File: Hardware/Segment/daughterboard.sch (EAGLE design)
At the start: 162 parts, among them IC1 PBQ79656PAPTQ1, IC2 PBQ79656PAPTQ1, T1 PBHV8115X, 115, T2 PBHV8115X, 115

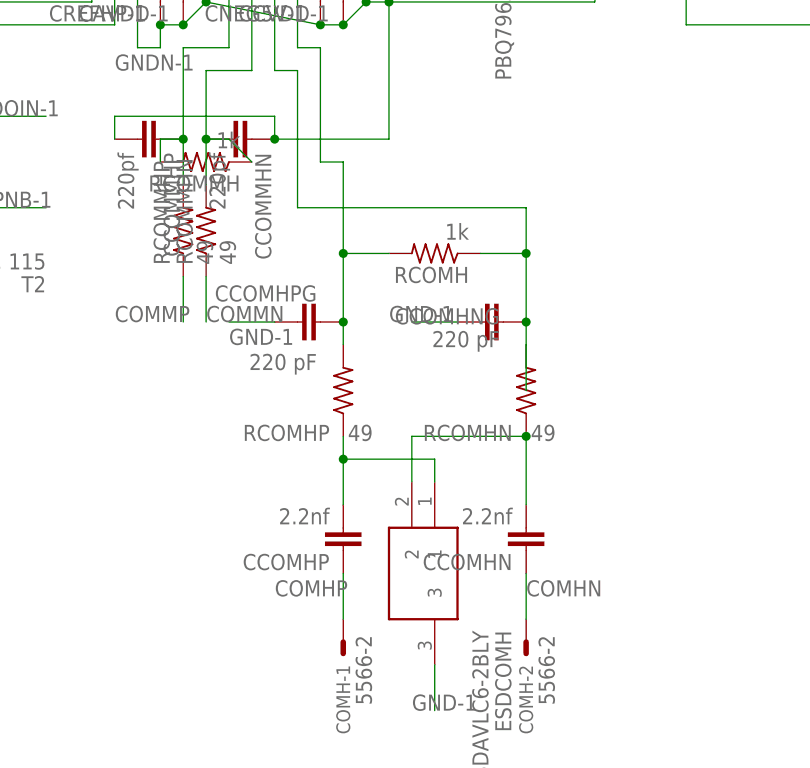
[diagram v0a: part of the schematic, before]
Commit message: Worked on routing daughterboard, mostly finished COM
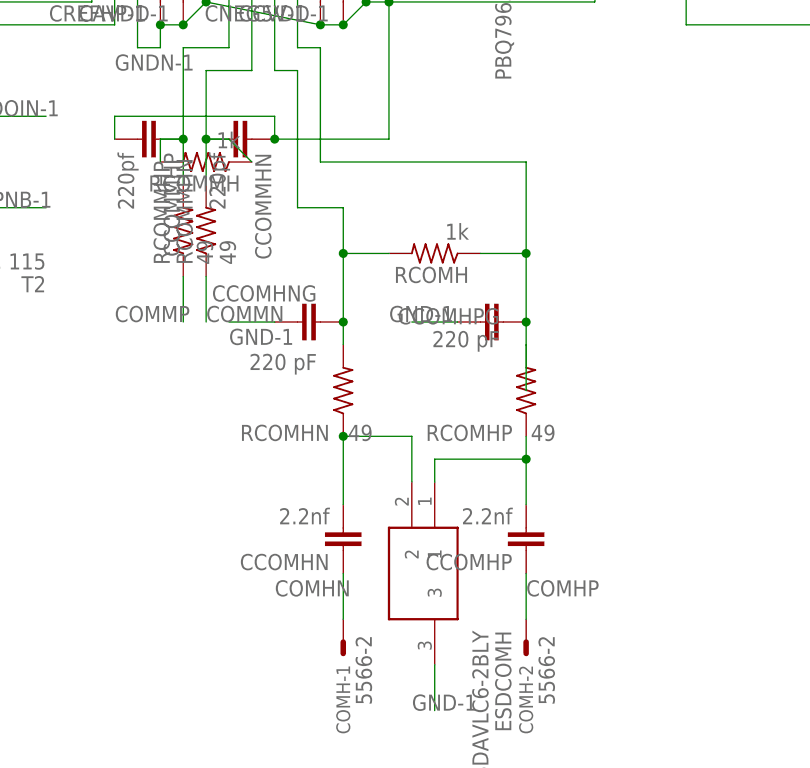
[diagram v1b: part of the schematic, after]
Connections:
- net COMHN: now also COMH-1.S; no longer COMH-2.S
- net COMHP: now also COMH-2.S; no longer COMH-1.S
- net N$131: now also RCOMH.1; no longer RCOMH.2
- net N$132: now also RCOMH.2; no longer RCOMH.1
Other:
- moved on the sheet: CCOMHN, CCOMHNG, CCOMHP, CCOMHPG, RCOMHN, RCOMHP

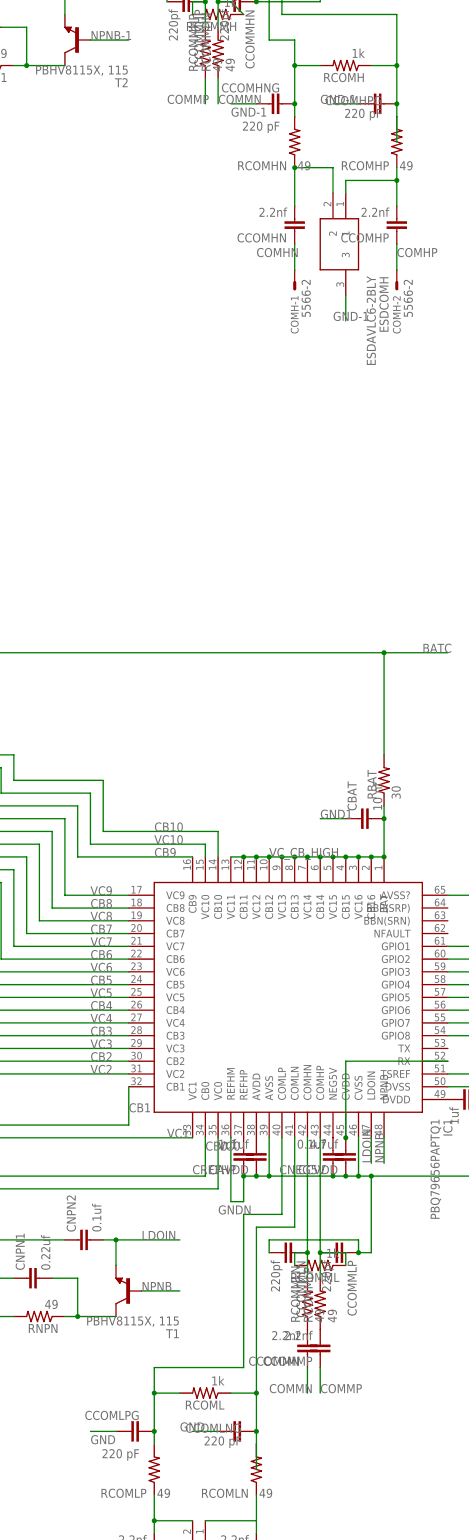
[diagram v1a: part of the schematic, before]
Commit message: Added com isolation to main board
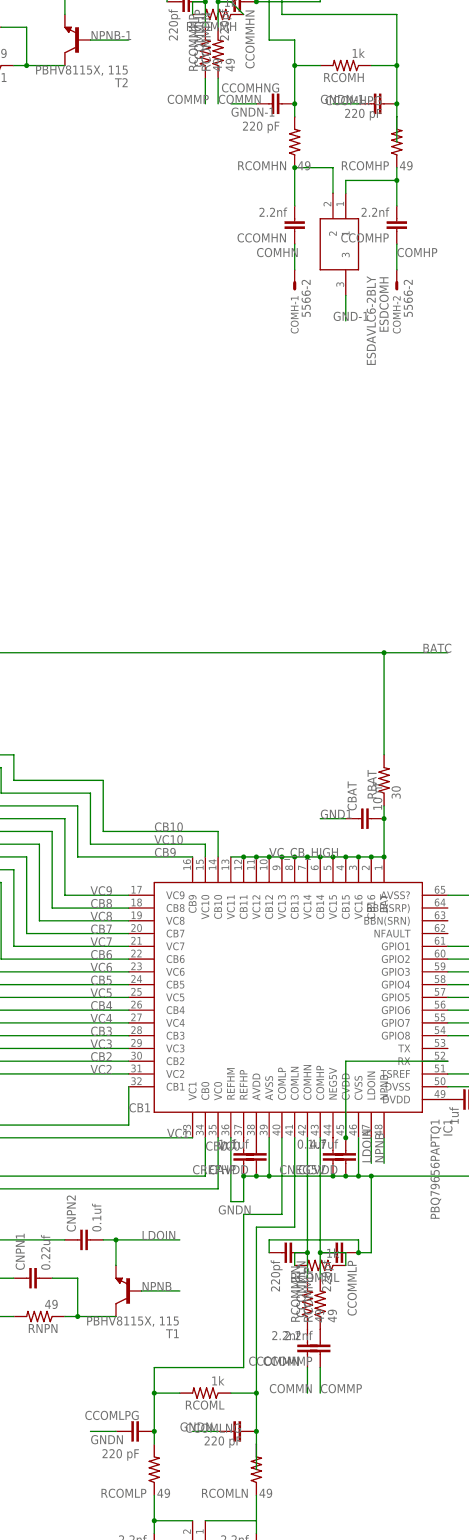
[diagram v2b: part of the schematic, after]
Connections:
- net GND: no longer CCOMLNG.1, CCOMLPG.1
- net GND-1: no longer CCOMHNG.1, CCOMHPG.1
- net GNDN: now also CCOMLNG.1, CCOMLPG.1
- net GNDN-1: now also CCOMHNG.1, CCOMHPG.1
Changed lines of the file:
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@@
 <junction x="175.26" y="20.32"/>
+</segment>
+<segment>
+<wire x1="124.46" y1="-30.48" x2="119.38" y2="-30.48" width="0.1524" layer="91"/>
+<label x="119.38" y="-33.02" size="1.778" layer="95"/>
+<pinref part="CCOMLPG" gate="G$1" pin="1"/>
+</segment>
+<segment>
+<pinref part="CCOMLNG" gate="G$1" pin="1"/>
+<wire x1="144.78" y1="-30.48" x2="139.7" y2="-30.48" width="0.1524" layer="91"/>
+<label x="137.16" y="-30.48" size="1.778" layer="95"/>
 </segment>
 </net>
@@
 <wire x1="104.14" y1="0" x2="93.98" y2="0" width="0.1524" layer="91"/>
 <label x="93.98" y="0" size="1.778" layer="95"/>
-</segment>
-<segment>
-<pinref part="CCOMLNG" gate="G$1" pin="1"/>
-<wire x1="144.78" y1="-30.48" x2="139.7" y2="-30.48" width="0.1524" layer="91"/>
-<label x="137.16" y="-30.48" size="1.778" layer="95"/>
-</segment>
-<segment>
-<wire x1="124.46" y1="-30.48" x2="119.38" y2="-30.48" width="0.1524" layer="91"/>
-<label x="119.38" y="-33.02" size="1.778" layer="95"/>
-<pinref part="CCOMLPG" gate="G$1" pin="1"/>
 </segment>
 <segment>
@@
 <wire x1="93.98" y1="248.92" x2="83.82" y2="248.92" width="0.1524" layer="91"/>
 <label x="83.82" y="248.92" size="1.778" layer="95"/>
-</segment>
-<segment>
-<pinref part="CCOMHPG" gate="G$1" pin="1"/>
-<wire x1="172.72" y1="233.68" x2="167.64" y2="233.68" width="0.1524" layer="91"/>
-<label x="165.1" y="233.68" size="1.778" layer="95"/>
-</segment>
-<segment>
-<wire x1="152.4" y1="233.68" x2="147.32" y2="233.68" width="0.1524" layer="91"/>
-<label x="147.32" y="231.14" size="1.778" layer="95"/>
-<pinref part="CCOMHNG" gate="G$1" pin="1"/>
 </segment>
 <segment>
@@
 <junction x="165.1" y="269.24"/>
 </segment>
-</net>
+<segment>
+<wire x1="152.4" y1="233.68" x2="147.32" y2="233.68" width="0.1524" layer="91"/>
+<label x="147.32" y="231.14" size="1.778" layer="95"/>
+<pinref part="CCOMHNG" gate="G$1" pin="1"/>
+</segment>
+<segment>
+<pinref part="CCOMHPG" gate="G$1" pin="1"/>
+<wire x1="172.72" y1="233.68" x2="167.64" y2="233.68" width="0.1524" layer="91"/>
+<label x="165.1" y="233.68" size="1.778" layer="95"/>
+</segment>
+</net>

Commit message: Ground planes on segment
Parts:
- added SR: 5566-2, con-molex:5566-2
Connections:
- removed net GND: CNPN1.1, ESDCOML.3
- removed net GND-1: CNPN1-1.1, ESDCOMH.3
- removed net GND1: CBAT.1, CBL-1.S, CTSREF1.1, RCB0.1, TEMPL-10.S, TEMPL-11.S, TEMPL-12.S, TEMPL-13.S, TEMPL-14.S, TEMPL-15.S, TEMPL-16.S, TEMPL-9.S
- removed net GND1-1: CBAT-1.1, CBH-1.S, CTSREF2.1, RCB0-1.1, TEMPH-10.S, TEMPH-11.S, TEMPH-12.S, TEMPH-13.S, TEMPH-14.S, TEMPH-15.S, TEMPH-16.S, TEMPH-9.S
- removed net GNDN: CAVDD.1, CCOMLNG.1, CCOMLPG.1, CCOMMLN.2, CCOMMLP.1, CCVDD.1, CDVDD.1, CNEG5V.1, CNPN2.1, CREFHP.1, IC1.AVSS, IC1.AVSS?, IC1.CVSS, IC1.DVSS, IC1.REFHM
- removed net GNDN-1: CAVDD-1.1, CCOMHNG.1, CCOMHPG.1, CCOMMHN.1, CCOMMHP.2, CCVDD-1.1, CDVDD-1.1, CNEG5V-1.1, CNPN2-1.1, CREFHP-1.1, IC2.AVSS, IC2.AVSS?, IC2.CVSS, IC2.DVSS, IC2.REFHM
- new net GNDH: CAVDD-1.1, CBAT-1.1, CBH-1.S, CCOMHNG.1, CCOMHPG.1, CCOMMHN.1, CCOMMHP.2, CCVDD-1.1, CDVDD-1.1, CNEG5V-1.1, CNPN1-1.1, CNPN2-1.1, CREFHP-1.1, CTSREF2.1, ESDCOMH.3, IC2.AVSS, IC2.AVSS?, IC2.CVSS, IC2.DVSS, IC2.REFHM, RCB0-1.1, TEMPH-10.S, TEMPH-11.S, TEMPH-12.S, TEMPH-13.S, TEMPH-14.S, TEMPH-15.S, TEMPH-16.S, TEMPH-9.S
- new net GNDL: CAVDD.1, CBAT.1, CBL-1.S, CCOMLNG.1, CCOMLPG.1, CCOMMLN.2, CCOMMLP.1, CCVDD.1, CDVDD.1, CNEG5V.1, CNPN1.1, CNPN2.1, CREFHP.1, CTSREF1.1, ESDCOML.3, IC1.AVSS, IC1.AVSS?, IC1.CVSS, IC1.DVSS, IC1.REFHM, RCB0.1, TEMPL-10.S, TEMPL-11.S, TEMPL-12.S, TEMPL-13.S, TEMPL-14.S, TEMPL-15.S, TEMPL-16.S, TEMPL-9.S
- new net N$4: IC1.BBP(SRP), SR-1.S
- new net N$7: IC1.BBN(SRN), SR-2.S

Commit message: Board and schematic are consistent, mostly wired, some problems
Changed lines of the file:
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@@
 <wire x1="228.6" y1="76.2" x2="238.76" y2="76.2" width="0.1524" layer="91"/>
 <label x="200.66" y="40.64" size="1.778" layer="95"/>
+<junction x="228.6" y="60.96"/>
 </segment>
 </net>
@@
 <junction x="152.4" y="-22.86"/>
 <wire x1="152.4" y1="-30.48" x2="152.4" y2="-33.02" width="0.1524" layer="91"/>
-<wire x1="152.4" y1="-33.02" x2="152.4" y2="-38.1" width="0.1524" layer="91"/>
 <pinref part="CCOMLNG" gate="G$1" pin="2"/>
 <junction x="152.4" y="-30.48"/>
@@
 <wire x1="152.4" y1="-48.26" x2="142.24" y2="-48.26" width="0.1524" layer="91"/>
 <pinref part="ESDCOML" gate="G$1" pin="1"/>
+<junction x="152.4" y="-48.26"/>
 </segment>
 </net>
@@
 <wire x1="218.44" y1="325.12" x2="228.6" y2="325.12" width="0.1524" layer="91"/>
 <label x="190.5" y="289.56" size="1.778" layer="95"/>
+<junction x="218.44" y="309.88"/>
 </segment>
 </net>
@@
 <wire x1="180.34" y1="233.68" x2="180.34" y2="231.14" width="0.1524" layer="91"/>
 <pinref part="RCOMHP" gate="G$1" pin="2"/>
-<wire x1="180.34" y1="231.14" x2="180.34" y2="226.06" width="0.1524" layer="91"/>
 <wire x1="157.48" y1="251.46" x2="180.34" y2="251.46" width="0.1524" layer="91"/>
 <wire x1="180.34" y1="251.46" x2="180.34" y2="241.3" width="0.1524" layer="91"/>
@@
 <pinref part="IC1" gate="G$1" pin="BBP(SRP)"/>
 <wire x1="190.5" y1="73.66" x2="190.5" y2="86.36" width="0.1524" layer="91"/>
-<wire x1="190.5" y1="86.36" x2="187.96" y2="86.36" width="0.1524" layer="91"/>
 <pinref part="SR" gate="-1" pin="S"/>
 <wire x1="190.5" y1="86.36" x2="193.04" y2="86.36" width="0.1524" layer="91"/>
@@
 </sheet>
 </sheets>
+<errors>
+</errors>
 </schematic>
 </drawing>

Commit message: Labeled a couple things in segment schematic
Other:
- note added: "External com"
- note added: "Internal com"
- note added: "Thermistor connections"
- note added: "Voltage sense and cell balancing connectors 0-10"
- note added: "Voltage sense and cell balancing connectors 10-20"
- note added: "Voltage source"
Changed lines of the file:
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@@
 <sheet>
 <plain>
+<text x="-22.86" y="71.12" size="1.778" layer="91">Voltage sense and cell balancing connectors 0-10</text>
+<text x="-45.72" y="322.58" size="1.778" layer="91">Voltage sense and cell balancing connectors 10-20</text>
+<text x="124.46" y="-78.74" size="1.778" layer="91">External com</text>
+<text x="157.48" y="182.88" size="1.778" layer="91">External com</text>
+<text x="132.08" y="231.14" size="1.778" layer="91">Internal com</text>
+<text x="162.56" y="-25.4" size="1.778" layer="91">Internal com</text>
+<text x="129.54" y="2.54" size="1.778" layer="91">Voltage source</text>
+<text x="116.84" y="251.46" size="1.778" layer="91">Voltage source</text>
+<text x="274.32" y="307.34" size="1.778" layer="91">Thermistor connections</text>
 </plain>
 <instances>

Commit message: Dummy battery and daughterboard v1.1
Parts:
- added DISABLE_UART: Disable UART, jumper:SJ
- added GND, RX, TX: (no value), wirepad:2,54/1,0
- added GNDH, GNDL: (no value), wirepad:SMD5
- added NFAULT: TPB2,54, testpad:TPB2,54
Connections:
- new net N$10: IC1.NFAULT, NFAULT.TP
- new net N$3: DISABLE_UART.2, IC1.RX, RX.P
- new net N$9: IC1.TX, TX.P
- net CVDD: now also DISABLE_UART.1; no longer IC1.RX
- net GNDH: now also GNDH.P
- net GNDL: now also GND.P, GNDL.P
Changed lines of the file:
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@@
 <part name="COMH" library="con-molex" library_urn="urn:adsk.eagle:library:165" deviceset="5566-2" device="" package3d_urn="urn:adsk.eagle:package:8078583/1"/>
 <part name="SR" library="con-molex" library_urn="urn:adsk.eagle:library:165" deviceset="5566-2" device="" package3d_urn="urn:adsk.eagle:package:8078583/1"/>
+<part name="DISABLE_UART" library="jumper" library_urn="urn:adsk.eagle:library:252" deviceset="SJ" device="" package3d_urn="urn:adsk.eagle:package:15471/1" value="Disable UART"/>
+<part name="GNDL" library="wirepad" library_urn="urn:adsk.eagle:library:412" deviceset="SMD5" device="" package3d_urn="urn:adsk.eagle:package:30841/1"/>
+<part name="GNDH" library="wirepad" library_urn="urn:adsk.eagle:library:412" deviceset="SMD5" device="" package3d_urn="urn:adsk.eagle:package:30841/1"/>
+<part name="TX" library="wirepad" library_urn="urn:adsk.eagle:library:412" deviceset="2,54/1,0" device="" package3d_urn="urn:adsk.eagle:package:30828/1"/>
+<part name="RX" library="wirepad" library_urn="urn:adsk.eagle:library:412" deviceset="2,54/1,0" device="" package3d_urn="urn:adsk.eagle:package:30828/1"/>
+<part name="GND" library="wirepad" library_urn="urn:adsk.eagle:library:412" deviceset="2,54/1,0" device="" package3d_urn="urn:adsk.eagle:package:30828/1"/>
+<part name="NFAULT" library="testpad" library_urn="urn:adsk.eagle:library:385" deviceset="TP" device="B2,54" package3d_urn="urn:adsk.eagle:package:27948/1"/>
 </parts>
 <sheets>
@@
 <attribute name="VALUE" x="194.818" y="82.677" size="1.778" layer="96"/>
 </instance>
+<instance part="DISABLE_UART" gate="1" x="175.26" y="43.18" smashed="yes">
+<attribute name="NAME" x="172.72" y="45.72" size="1.778" layer="95"/>
+<attribute name="VALUE" x="172.72" y="39.37" size="1.778" layer="96"/>
+</instance>
+<instance part="GNDL" gate="1" x="152.4" y="17.78" smashed="yes" rot="R180">
+<attribute name="NAME" x="153.543" y="15.9258" size="1.778" layer="95" rot="R180"/>
+<attribute name="VALUE" x="153.543" y="21.082" size="1.778" layer="96" rot="R180"/>
+</instance>
+<instance part="GNDH" gate="1" x="144.78" y="266.7" smashed="yes" rot="R180">
+<attribute name="NAME" x="145.923" y="264.8458" size="1.778" layer="95" rot="R180"/>
+<attribute name="VALUE" x="145.923" y="270.002" size="1.778" layer="96" rot="R180"/>
+</instance>
+<instance part="TX" gate="P" x="195.58" y="45.72" smashed="yes" rot="R180">
+<attribute name="NAME" x="196.723" y="43.8658" size="1.778" layer="95" rot="R180"/>
+<attribute name="VALUE" x="196.723" y="49.022" size="1.778" layer="96" rot="R180"/>
+</instance>
+<instance part="RX" gate="P" x="195.58" y="43.18" smashed="yes" rot="R180">
+<attribute name="NAME" x="196.723" y="41.3258" size="1.778" layer="95" rot="R180"/>
+<attribute name="VALUE" x="196.723" y="46.482" size="1.778" layer="96" rot="R180"/>
+</instance>
+<instance part="GND" gate="P" x="195.58" y="17.78" smashed="yes" rot="R90">
+<attribute name="NAME" x="193.7258" y="16.637" size="1.778" layer="95" rot="R90"/>
+<attribute name="VALUE" x="198.882" y="16.637" size="1.778" layer="96" rot="R90"/>
+</instance>
+<instance part="NFAULT" gate="G$1" x="193.04" y="68.58" smashed="yes" rot="R270">
+<attribute name="NAME" x="194.31" y="69.85" size="1.778" layer="95" rot="R270"/>
+<attribute name="TP_SIGNAL_NAME" x="191.77" y="67.31" size="1.778" layer="97" rot="R270"/>
+</instance>
 </instances>
 <busses>
@@
 <pinref part="CREFHP" gate="G$1" pin="1"/>
 <wire x1="147.32" y1="15.24" x2="149.86" y2="15.24" width="0.1524" layer="91"/>
-<wire x1="149.86" y1="15.24" x2="149.86" y2="20.32" width="0.1524" layer="91"/>
+<wire x1="149.86" y1="15.24" x2="149.86" y2="17.78" width="0.1524" layer="91"/>
 <pinref part="IC1" gate="G$1" pin="AVSS"/>
+<wire x1="149.86" y1="17.78" x2="149.86" y2="20.32" width="0.1524" layer="91"/>
 <wire x1="154.94" y1="27.94" x2="154.94" y2="20.32" width="0.1524" layer="91"/>
 <pinref part="CAVDD" gate="G$1" pin="1"/>
@@
 <wire x1="198.12" y1="38.1" x2="198.12" y2="35.56" width="0.1524" layer="91"/>
 <wire x1="198.12" y1="35.56" x2="198.12" y2="20.32" width="0.1524" layer="91"/>
-<wire x1="198.12" y1="20.32" x2="175.26" y2="20.32" width="0.1524" layer="91"/>
+<wire x1="198.12" y1="20.32" x2="195.58" y2="20.32" width="0.1524" layer="91"/>
 <junction x="198.12" y="35.56"/>
 <junction x="172.72" y="20.32"/>
 <pinref part="IC1" gate="G$1" pin="AVSS?"/>
+<wire x1="195.58" y1="20.32" x2="175.26" y2="20.32" width="0.1524" layer="91"/>
 <wire x1="175.26" y1="20.32" x2="172.72" y2="20.32" width="0.1524" layer="91"/>
 <wire x1="190.5" y1="76.2" x2="198.12" y2="76.2" width="0.1524" layer="91"/>
@@
 <junction x="172.72" y="5.08"/>
 <junction x="175.26" y="20.32"/>
+<pinref part="GNDL" gate="1" pin="P"/>
+<junction x="149.86" y="17.78"/>
+<pinref part="GND" gate="P" pin="P"/>
+<junction x="195.58" y="20.32"/>
 </segment>
 <segment>
@@
 <net name="CVDD" class="0">
 <segment>
-<pinref part="IC1" gate="G$1" pin="RX"/>
-<wire x1="190.5" y1="43.18" x2="170.18" y2="43.18" width="0.1524" layer="91"/>
 <pinref part="CCVDD" gate="G$1" pin="2"/>
 <pinref part="IC1" gate="G$1" pin="CVDD"/>
 <wire x1="170.18" y1="43.18" x2="170.18" y2="27.94" width="0.1524" layer="91"/>
 <junction x="170.18" y="27.94"/>
+<pinref part="DISABLE_UART" gate="1" pin="1"/>
 </segment>
 </net>
@@
 <net name="CVDD-1" class="0">
 <segment>
-<pinref part="IC2" gate="G$1" pin="RX"/>
-<wire x1="180.34" y1="292.1" x2="160.02" y2="292.1" width="0.1524" layer="91"/>
 <pinref part="CCVDD-1" gate="G$1" pin="2"/>
 <pinref part="IC2" gate="G$1" pin="CVDD"/>
@@
 <junction x="160.02" y="274.32"/>
 <wire x1="160.02" y1="274.32" x2="160.02" y2="276.86" width="0.1524" layer="91"/>
+<pinref part="IC2" gate="G$1" pin="RX"/>
+<wire x1="180.34" y1="292.1" x2="160.02" y2="292.1" width="0.1524" layer="91"/>
 </segment>
 </net>
@@
 <junction x="152.4" y="254"/>
 <junction x="165.1" y="269.24"/>
+<pinref part="GNDH" gate="1" pin="P"/>
 </segment>
 <segment>
@@
 </segment>
 </net>
+<net name="N$3" class="0">
+<segment>
+<pinref part="DISABLE_UART" gate="1" pin="2"/>
+<pinref part="IC1" gate="G$1" pin="RX"/>
+<wire x1="180.34" y1="43.18" x2="190.5" y2="43.18" width="0.1524" layer="91"/>
+<wire x1="193.04" y1="43.18" x2="190.5" y2="43.18" width="0.1524" layer="91"/>
+<pinref part="RX" gate="P" pin="P"/>
+</segment>
+</net>
+<net name="N$9" class="0">
+<segment>
+<pinref part="IC1" gate="G$1" pin="TX"/>
+<wire x1="193.04" y1="45.72" x2="190.5" y2="45.72" width="0.1524" layer="91"/>
+<pinref part="TX" gate="P" pin="P"/>
+</segment>
+</net>
+<net name="N$10" class="0">
+<segment>
+<pinref part="IC1" gate="G$1" pin="NFAULT"/>
+<pinref part="NFAULT" gate="G$1" pin="TP"/>
+</segment>
+</net>

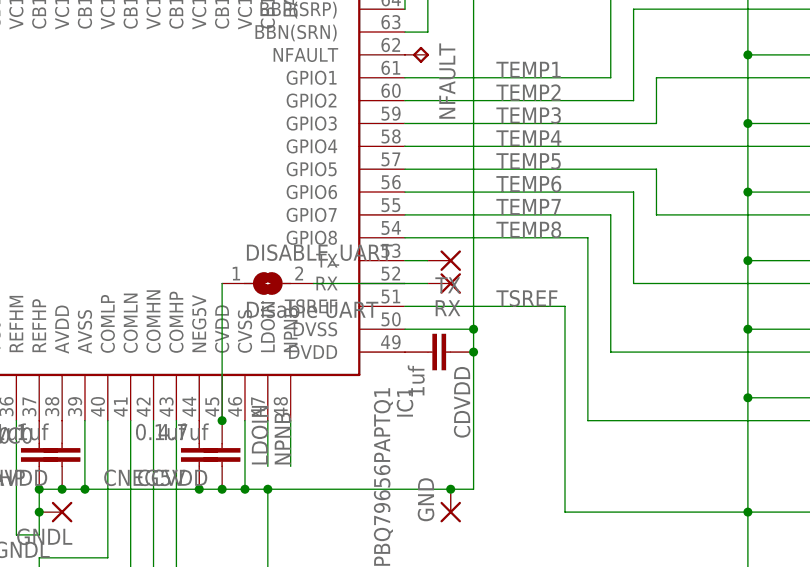
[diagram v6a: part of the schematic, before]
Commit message: Rotated connector to shrink board
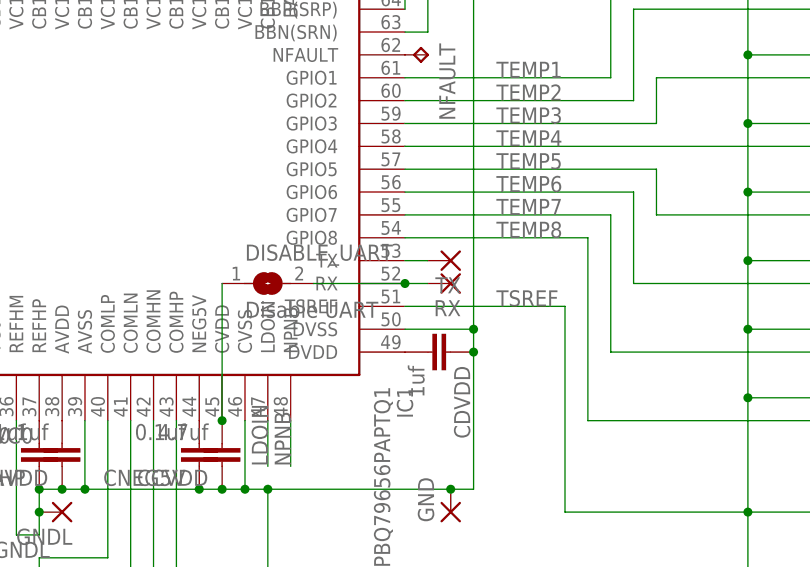
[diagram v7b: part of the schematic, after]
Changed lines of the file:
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@@
 <wire x1="193.04" y1="43.18" x2="190.5" y2="43.18" width="0.1524" layer="91"/>
 <pinref part="RX" gate="P" pin="P"/>
+<junction x="190.5" y="43.18"/>
 </segment>
 </net>
